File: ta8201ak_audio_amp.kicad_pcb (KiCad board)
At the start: 2 copper layers, 39.4 x 29.9 mm, 24 parts, among them J1 IN, J2 RV1_3, J3 RV1_2, J4 Out1, J5 Out2, J6 Vcc, J7 Gnd, J8 SW1_1, J9 SW1_2

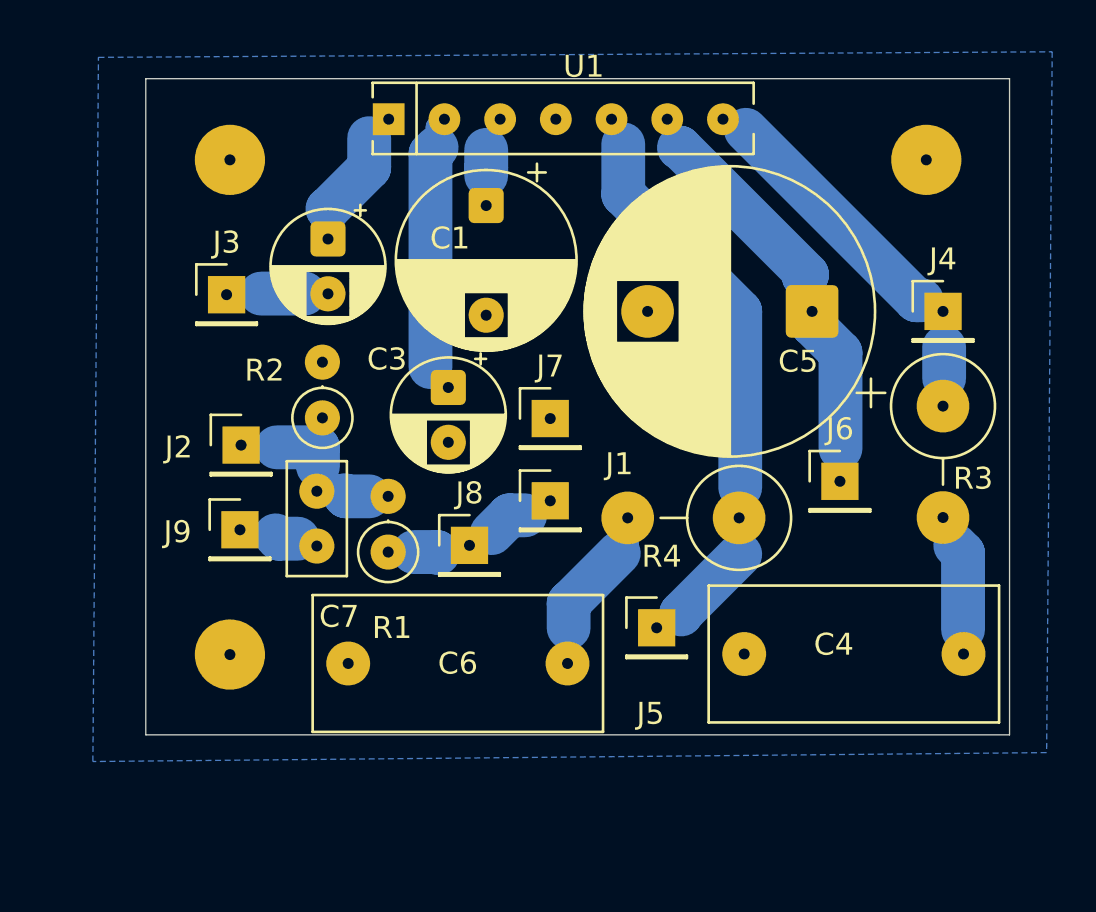
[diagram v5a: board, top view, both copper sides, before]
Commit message: ベタGNDをやめ、音声がICに入るまでのGNDと電源のGNDを分離した。
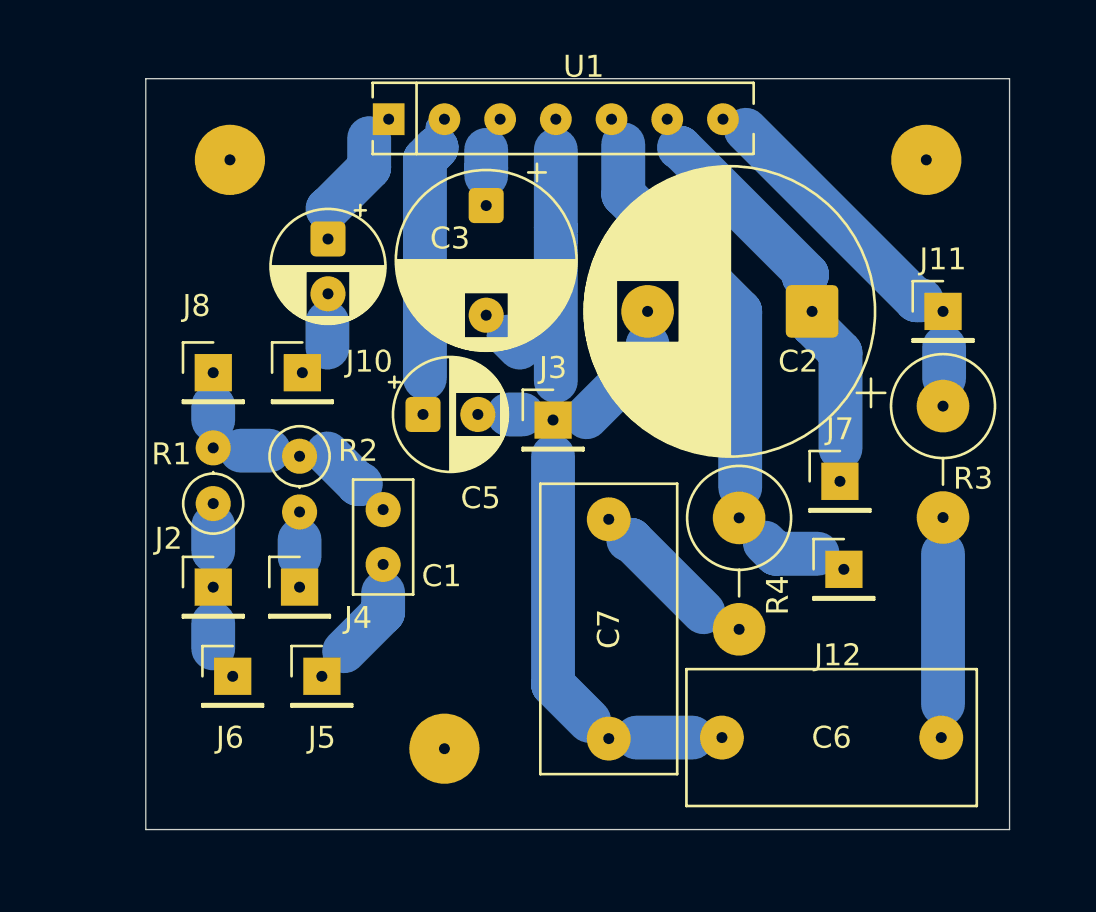
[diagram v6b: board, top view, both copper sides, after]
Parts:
- removed the C4 at (190.7, 79.4)
- removed the C7 at (161.2, 74.5)
- removed the J7 at (171.8, 68.6)
- added C1: 100p, Capacitor_THT:C_Disc_D5.0mm_W2.5mm_P2.50mm, F.Cu at (164.2, 75.3)
- added C6: 0.15u, Capacitor_THT:C_Rect_L13.0mm_W6.0mm_P10.00mm_FKS3_FKP3_MKS4, F.Cu at (189.7, 83.2)
- added J3: Gnd, Connector_PinHeader_2.54mm:PinHeader_1x01_P2.54mm_Vertical, F.Cu at (172.0, 68.7)
- added J4: AudioGnd, Connector_PinHeader_2.54mm:PinHeader_1x01_P2.54mm_Vertical, F.Cu at (160.4, 76.3)
- moved J2 15.9 mm to (156.5, 76.3)
- moved J6 12.3 mm to (157.4, 80.4)
- moved H3 10.7 mm to (167.0, 83.7)
- moved J12 8.94 mm to (185.2, 75.5)
- moved R1 8.28 mm to (156.5, 72.5)
- moved J5 7.65 mm to (161.4, 80.4)
- moved C7 6.84 mm to (174.5, 73.2), turned to -90 degrees
- moved J10 4.96 mm to (160.5, 66.5)
- moved J8 3.54 mm to (156.5, 66.5)
- moved R2 2.04 mm to (160.4, 70.4), turned to -90 degrees
- moved C5 1.69 mm to (166.0, 68.5), turned to 0 degrees
- turned R4 to -90 degrees
- renumbered C5 to C2, C1 to C3, C2 to C4, C3 to C5, C6 to C7, J3 to J10, J4 to J11, J5 to J12, J1 to J2, J9 to J5, J8 to J6, J6 to J7, J2 to J8
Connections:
- R2 pad 2: GND -> GND2
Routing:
- net GND: track 0.00 -> 39.8 mm
- net Net-(C6-Pad1): track 5.11 -> 8.51 mm
- net Net-(J12-Pin_1): track 25.0 -> 22.4 mm
- net Net-(J5-Pin_1): track 2.08 -> 4.69 mm
- net Net-(J8-Pin_1): track 5.83 -> 7.92 mm
- net GND2: track 0.00 -> 2.03 mm
- net Net-(C7-Pad1): track 7.77 -> 6.10 mm
- net Net-(U1-NF): track 11.6 -> 12.6 mm
- removed copper zone on B.Cu, net GND
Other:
- board size 39.4 x 29.9 mm -> 39.4 x 34.2 mm

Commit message: パッド: 円形 Φ2.0 / 四角 2.0×2.0 / SIP 1.6×2.2 配線: 電源 2.0 / 信号 1.5 クリアランス: 0.5 ティアドロップ適用 ネジ穴をスルーホールにして真ん中が白抜きになるように 直角を排除
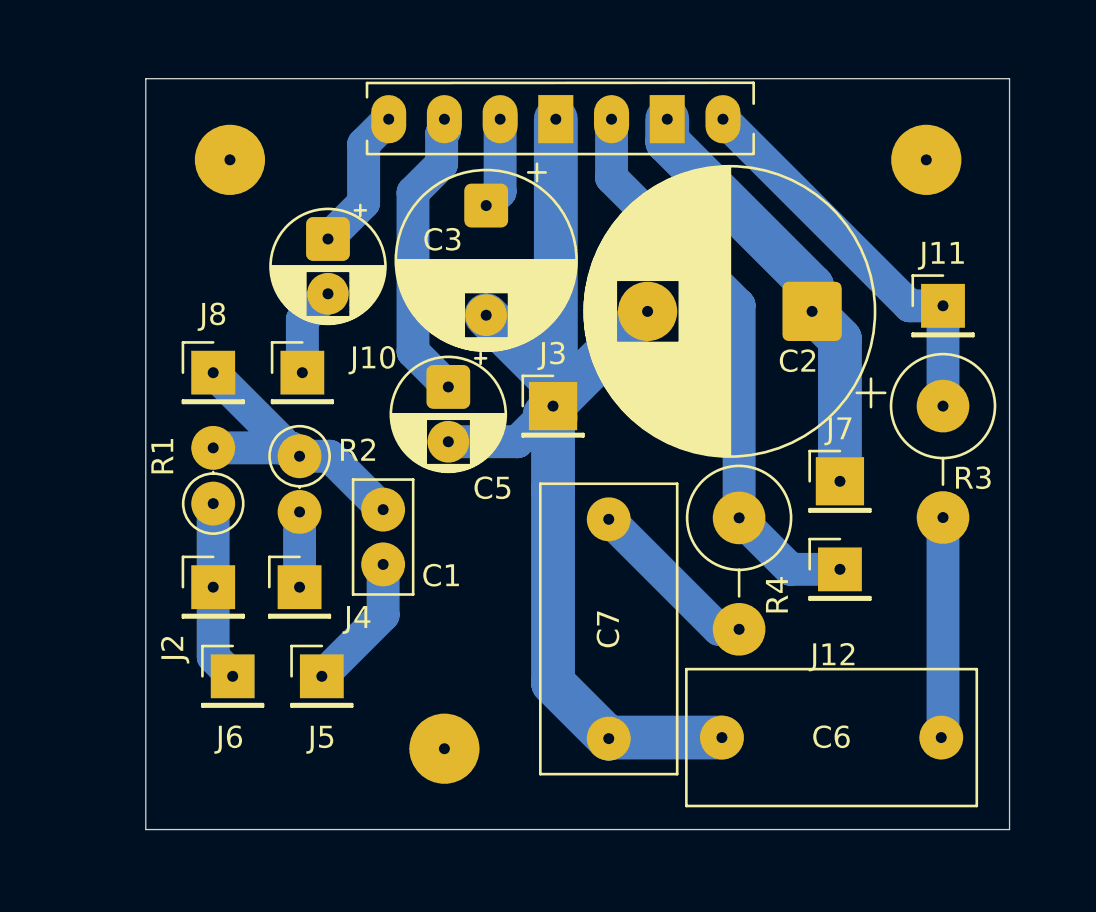
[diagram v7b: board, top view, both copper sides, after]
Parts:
- moved C5 1.71 mm to (167.2, 67.2), turned to -90 degrees
- moved J3 0.63 mm to (172.0, 68.1)
- moved J11 0.25 mm to (189.7, 63.5)
- moved J12 0.18 mm to (185.0, 75.5)
- moved U1 0.11 mm to (172.1, 55.0)
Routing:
- net GND: track 39.8 -> 50.8 mm
- net Net-(J8-Pin_1): track 7.92 -> 13.6 mm
- net Net-(J12-Pin_1): track 22.4 -> 26.6 mm
- net Net-(J11-Pin_1): track 14.1 -> 18.4 mm
- net VCC: track 16.9 -> 20.4 mm
- net Net-(J2-Pin_1): track 4.95 -> 8.24 mm
- net Net-(U1-R.F): track 1.17 -> 4.20 mm
- net Net-(C7-Pad1): track 6.10 -> 8.07 mm
- net Net-(J5-Pin_1): track 4.69 -> 6.26 mm
- net Net-(C6-Pad1): track 8.51 -> 10.1 mm
- net Net-(J10-Pin_1): track 2.58 -> 4.08 mm
- net GND2: track 2.03 -> 3.43 mm
- net Net-(U1-IN): track 5.41 -> 6.61 mm
- net Net-(U1-NF): track 12.6 -> 13.5 mm

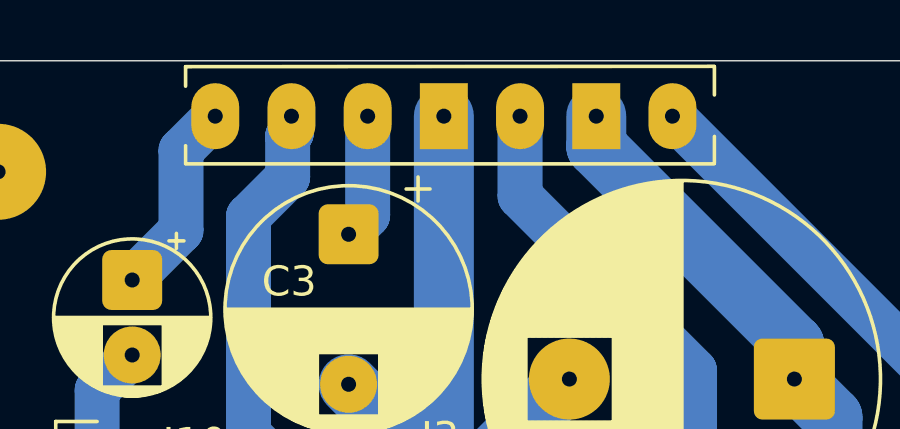
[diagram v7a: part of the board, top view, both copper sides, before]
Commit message: ICのフットプリントを修正
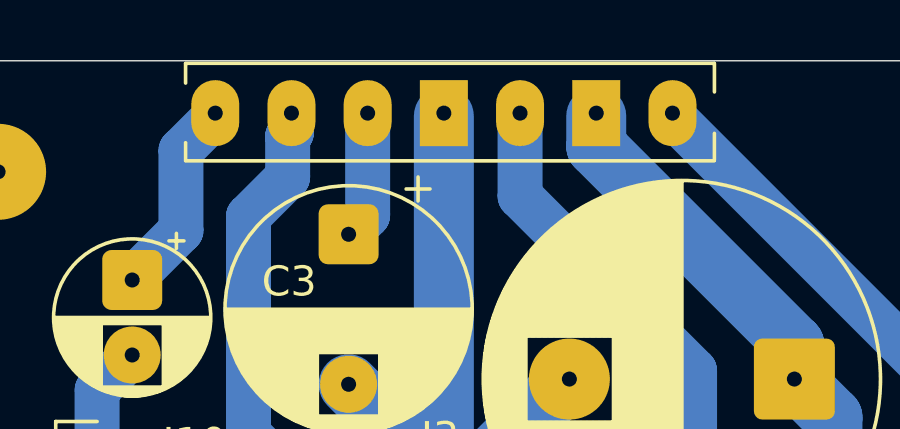
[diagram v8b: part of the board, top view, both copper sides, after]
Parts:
- moved U1 0.10 mm to (172.1, 54.9)
